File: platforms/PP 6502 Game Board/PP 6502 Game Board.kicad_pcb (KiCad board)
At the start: 2 copper layers, 99.1 x 99.1 mm, 33 parts, among them J1 BASE, J2 BTM, J3 TOP, J4 SBC, J5 TRS_3.5mm, M1 Mounting, M2 Mounting, M3 Mounting, M4 Mounting, Q1 2N2222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

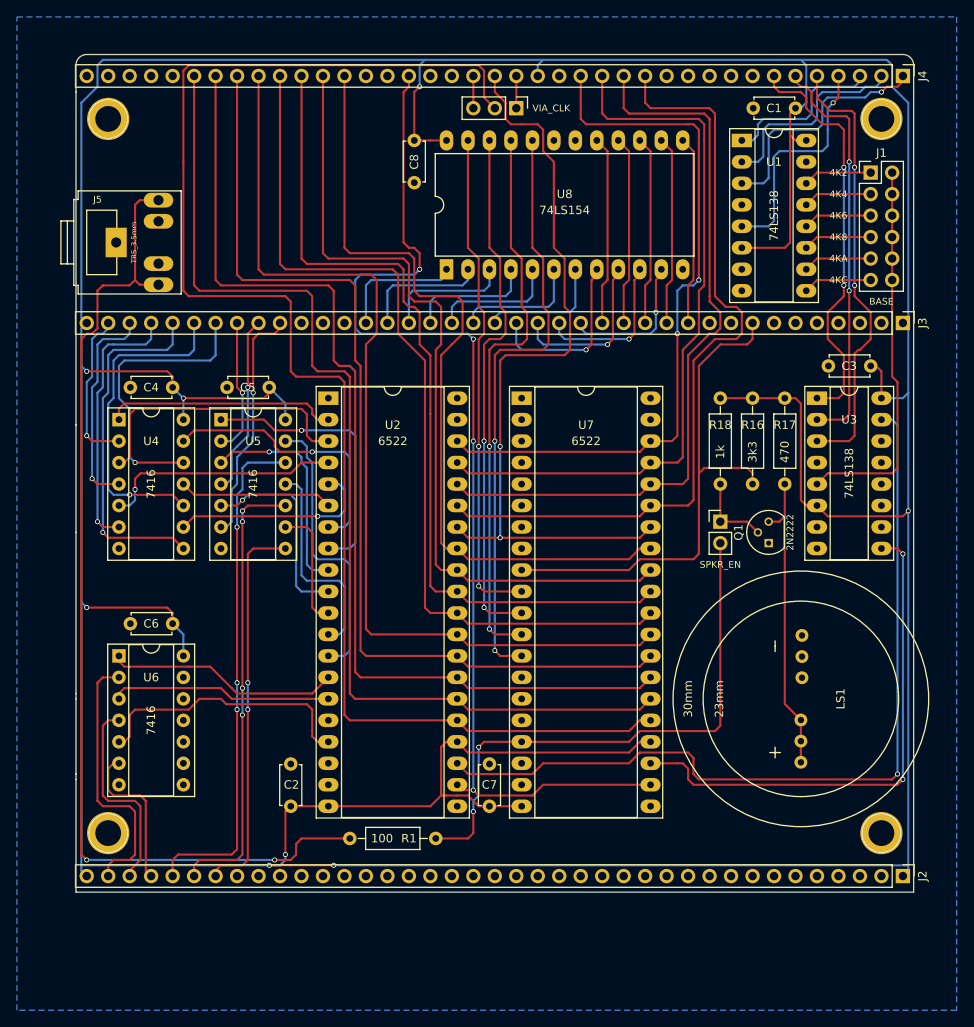
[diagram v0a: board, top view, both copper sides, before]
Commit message: Gameboard faceplate layout and logo
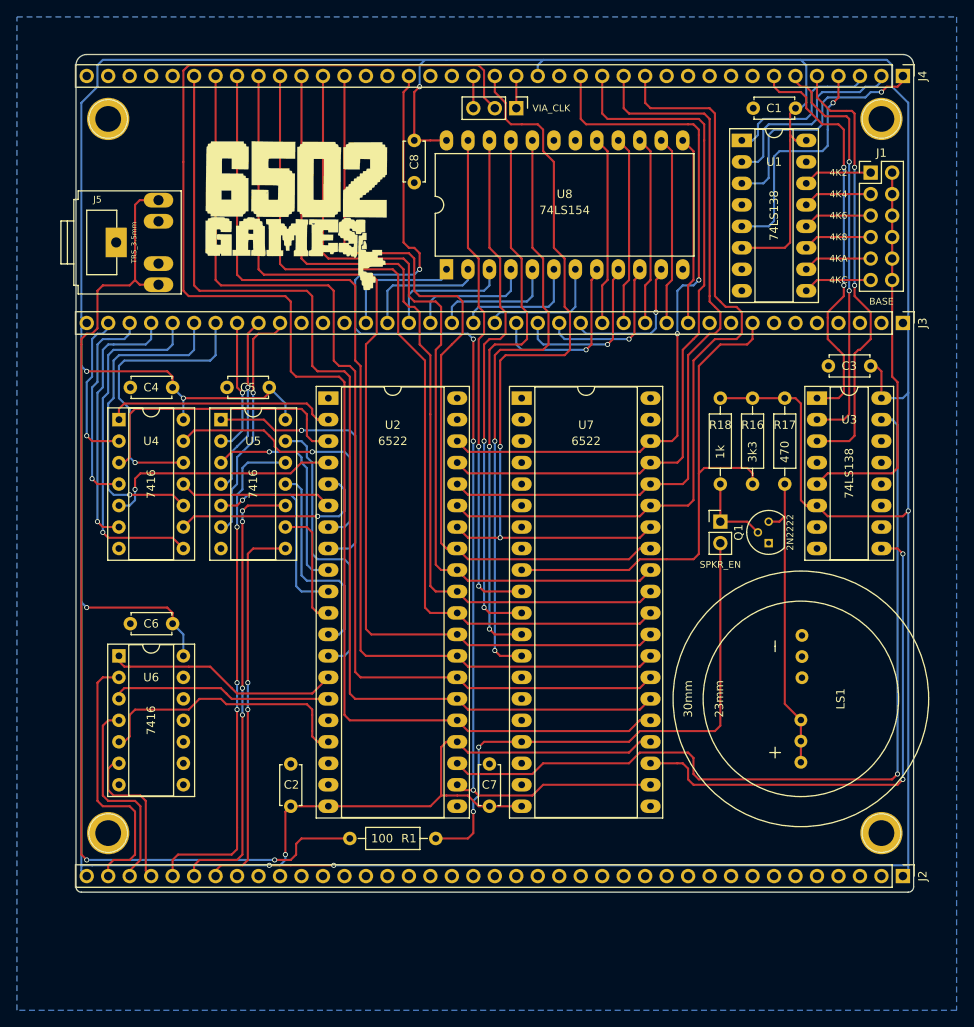
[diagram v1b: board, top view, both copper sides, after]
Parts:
- added G***: LOGO, logo:6502 games 2, F.Cu at (126.4, 67.3)
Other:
- outline, holes or cut-outs redrawn

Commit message: Added IRQ pin to 6502 Game Board
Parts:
- removed G***: LOGO, logo:6502 games 2
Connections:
- J4 pad 22: (no net) -> /~IRQ
- U7 pad 21: (no net) -> /~IRQ
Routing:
- net /~IRQ: track 0.00 -> 123.3 mm, vias 0 -> 4
- net /R/~W: track 129.9 -> 125.3 mm
- net /D3: track 105.4 -> 106.1 mm
- net /D0: track 94.9 -> 95.6 mm

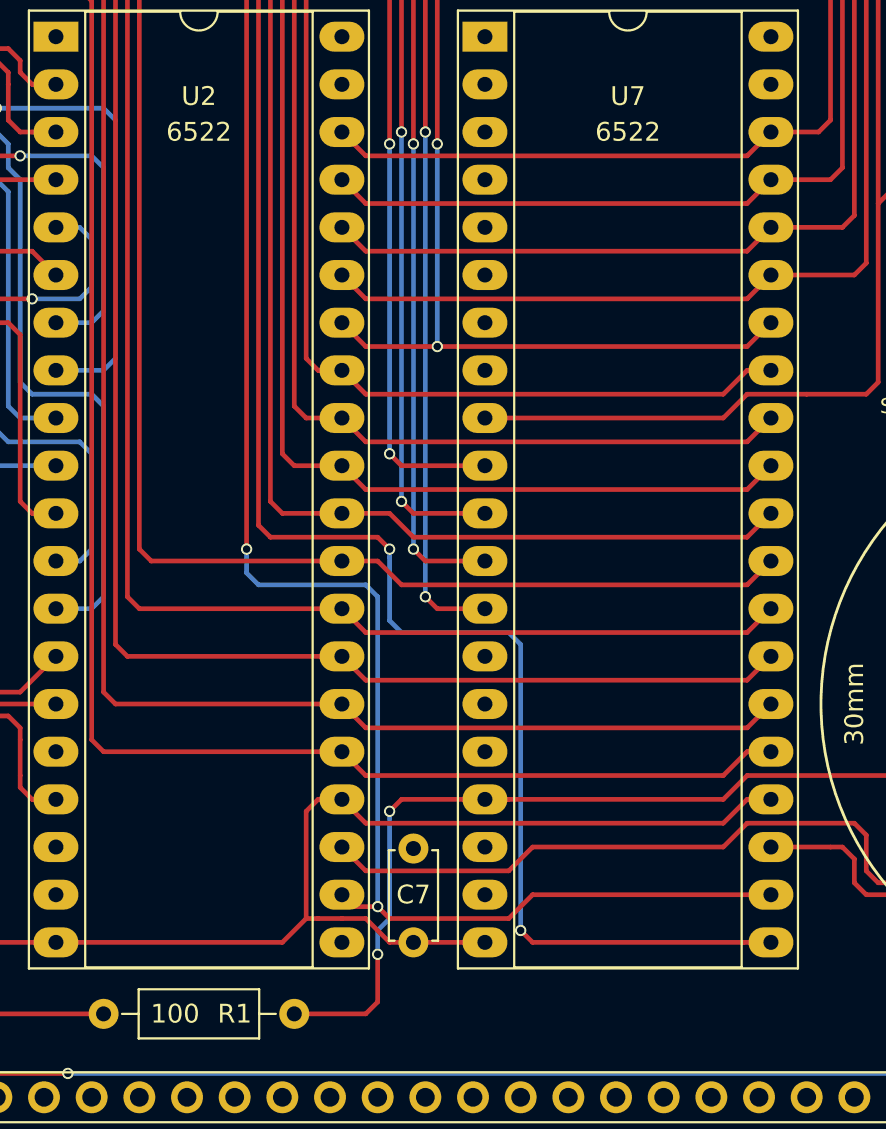
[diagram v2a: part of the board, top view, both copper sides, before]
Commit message: Moved game board IRQ connection to correct VIA
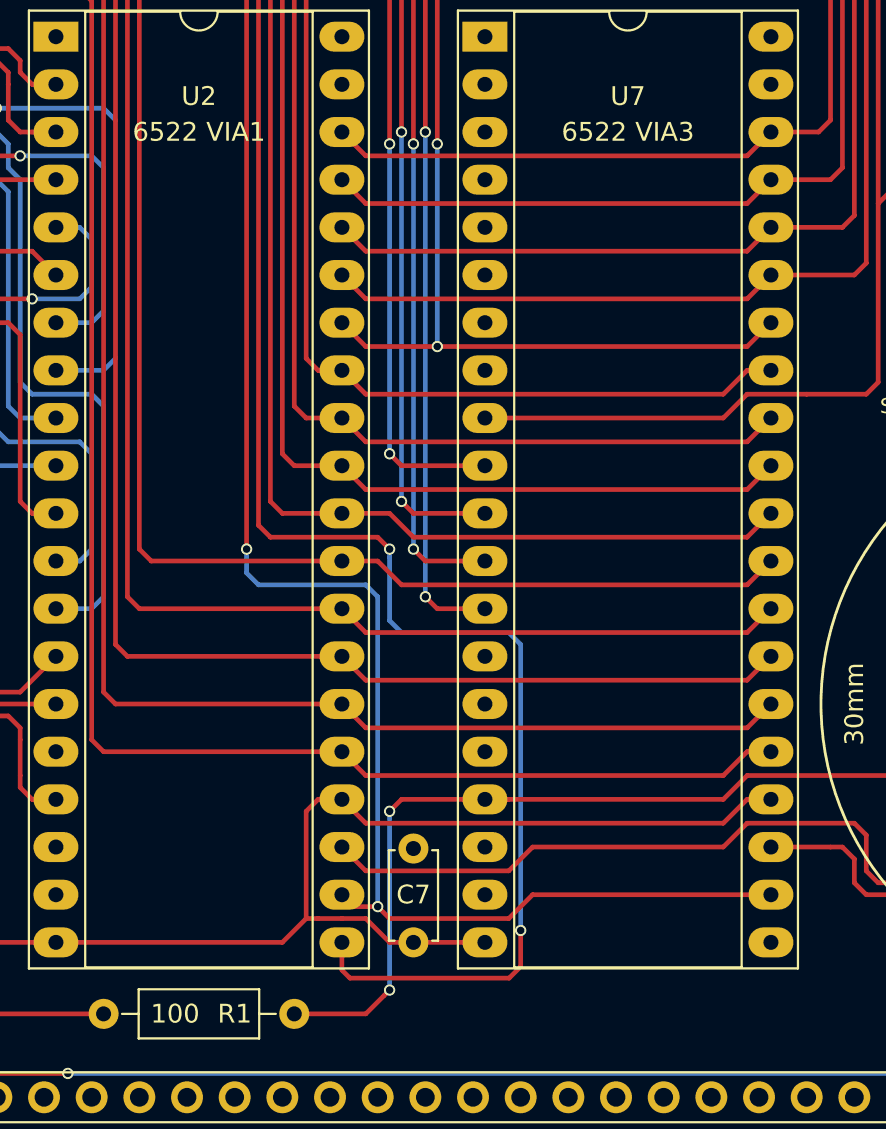
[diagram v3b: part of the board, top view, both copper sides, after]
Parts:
- U2: value 6522 -> 6522 VIA1
- U7: value 6522 -> 6522 VIA3
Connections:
- U2 pad 21: (no net) -> /~IRQ
- U7 pad 21: /~IRQ -> (no net)
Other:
- board text added: "VIA #3"
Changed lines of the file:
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@@
       (effects (font (size 1 1) (thickness 0.15)))
     )
-    (fp_text value 6522 (at 7.62 5.08 180) (layer F.SilkS)
+    (fp_text value "6522 VIA1" (at 7.62 5.08 180) (layer F.SilkS)
       (effects (font (size 1 1) (thickness 0.15)))
     )
@@
     (pad 1 thru_hole rect (at 0 0) (size 2.4 1.6) (drill 0.8) (layers *.Cu *.Mask)
       (net 1 GND))
-    (pad 21 thru_hole oval (at 15.24 48.26) (size 2.4 1.6) (drill 0.8) (layers *.Cu *.Mask))
+    (pad 21 thru_hole oval (at 15.24 48.26) (size 2.4 1.6) (drill 0.8) (layers *.Cu *.Mask)
+      (net 91 /~IRQ))
     (pad 2 thru_hole oval (at 0 2.54) (size 2.4 1.6) (drill 0.8) (layers *.Cu *.Mask)
       (net 24 "Net-(U2-Pad2)"))
@@
       (effects (font (size 1 1) (thickness 0.15)))
     )
-    (fp_text value 6522 (at 7.62 5.08) (layer F.SilkS)
+    (fp_text value "6522 VIA3" (at 7.62 5.08) (layer F.SilkS)
       (effects (font (size 1 1) (thickness 0.15)))
     )
@@
     (pad 1 thru_hole rect (at 0 0) (size 2.4 1.6) (drill 0.8) (layers *.Cu *.Mask)
       (net 1 GND))
-    (pad 21 thru_hole oval (at 15.24 48.26) (size 2.4 1.6) (drill 0.8) (layers *.Cu *.Mask)
-      (net 91 /~IRQ))
+    (pad 21 thru_hole oval (at 15.24 48.26) (size 2.4 1.6) (drill 0.8) (layers *.Cu *.Mask))
     (pad 2 thru_hole oval (at 0 2.54) (size 2.4 1.6) (drill 0.8) (layers *.Cu *.Mask))
     (pad 22 thru_hole oval (at 15.24 45.72) (size 2.4 1.6) (drill 0.8) (layers *.Cu *.Mask)
@@
     (effects (font (size 1 1) (thickness 0.15)) (justify mirror))
   )
-  (gr_text "6522 VIA" (at 160.655 93.98) (layer B.SilkS)
+  (gr_text "VIA #3" (at 160.655 93.98) (layer B.SilkS)
     (effects (font (size 1.5 1.5) (thickness 0.15)) (justify mirror))
   )
@@
   (segment (start 179.705 103.505) (end 180.975 104.775) (width 0.25) (layer F.Cu) (net 68) (status 20))
   (segment (start 153.035 129.54) (end 148.59 129.54) (width 0.25) (layer F.Cu) (net 69) (status 10))
-  (segment (start 146.685 140.97) (end 142.875 140.97) (width 0.25) (layer F.Cu) (net 69) (status 20))
-  (segment (start 147.32 140.335) (end 146.685 140.97) (width 0.25) (layer F.Cu) (net 69))
-  (segment (start 147.32 137.795) (end 147.32 140.335) (width 0.25) (layer F.Cu) (net 69))
-  (via (at 147.32 137.795) (size 0.6) (drill 0.4) (layers F.Cu B.Cu) (net 69))
-  (segment (start 147.32 136.525) (end 147.32 137.795) (width 0.25) (layer B.Cu) (net 69))
-  (segment (start 147.955 135.89) (end 147.32 136.525) (width 0.25) (layer B.Cu) (net 69))
-  (segment (start 147.955 130.175) (end 147.955 135.89) (width 0.25) (layer B.Cu) (net 69))
   (via (at 147.955 130.175) (size 0.6) (drill 0.4) (layers F.Cu B.Cu) (net 69))
   (segment (start 148.59 129.54) (end 147.955 130.175) (width 0.25) (layer F.Cu) (net 69))
@@
   (segment (start 158.115 83.82) (end 151.13 83.82) (width 0.25) (layer F.Cu) (net 90))
   (segment (start 151.13 83.82) (end 150.495 84.455) (width 0.25) (layer F.Cu) (net 90))
-  (segment (start 168.275 137.16) (end 166.825 137.16) (width 0.25) (layer F.Cu) (net 91))
+  (via (at 147.955 139.700014) (size 0.6) (drill 0.4) (layers F.Cu B.Cu) (net 69))
+  (segment (start 147.955 130.175) (end 147.955 139.700014) (width 0.25) (layer B.Cu) (net 69))
+  (segment (start 147.655001 140.000013) (end 147.955 139.700014) (width 0.25) (layer F.Cu) (net 69))
+  (segment (start 142.875 140.97) (end 146.685014 140.97) (width 0.25) (layer F.Cu) (net 69))
+  (segment (start 146.685014 140.97) (end 147.655001 140.000013) (width 0.25) (layer F.Cu) (net 69))
   (via (at 154.94 136.525) (size 0.6) (drill 0.4) (layers F.Cu B.Cu) (net 91))
-  (segment (start 166.825 137.16) (end 155.575 137.16) (width 0.25) (layer F.Cu) (net 91))
-  (segment (start 155.575 137.16) (end 154.94 136.525) (width 0.25) (layer F.Cu) (net 91))
   (via (at 147.955 116.205) (size 0.6) (drill 0.4) (layers F.Cu B.Cu) (net 91))
   (segment (start 147.955 116.629264) (end 147.955 116.205) (width 0.25) (layer B.Cu) (net 91))
@@
   (segment (start 142.875 66.04) (end 144.78 66.04) (width 0.25) (layer F.Cu) (net 91))
   (segment (start 144.78 66.04) (end 145.415 65.405) (width 0.25) (layer F.Cu) (net 91))
+  (segment (start 145.8425 139.065) (end 154.326501 139.065) (width 0.25) (layer F.Cu) (net 91))
+  (segment (start 154.94 138.451501) (end 154.94 136.525) (width 0.25) (layer F.Cu) (net 91))
+  (segment (start 154.326501 139.065) (end 154.94 138.451501) (width 0.25) (layer F.Cu) (net 91))
+  (segment (start 145.415 137.16) (end 145.415 138.6375) (width 0.25) (layer F.Cu) (net 91))
+  (segment (start 145.415 138.6375) (end 145.8425 139.065) (width 0.25) (layer F.Cu) (net 91))
   (zone (net 1) (net_name GND) (layer B.Cu) (hatch edge 0.508)
     (connect_pads (clearance 0.508))
